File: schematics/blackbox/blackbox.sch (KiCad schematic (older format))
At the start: 37 parts

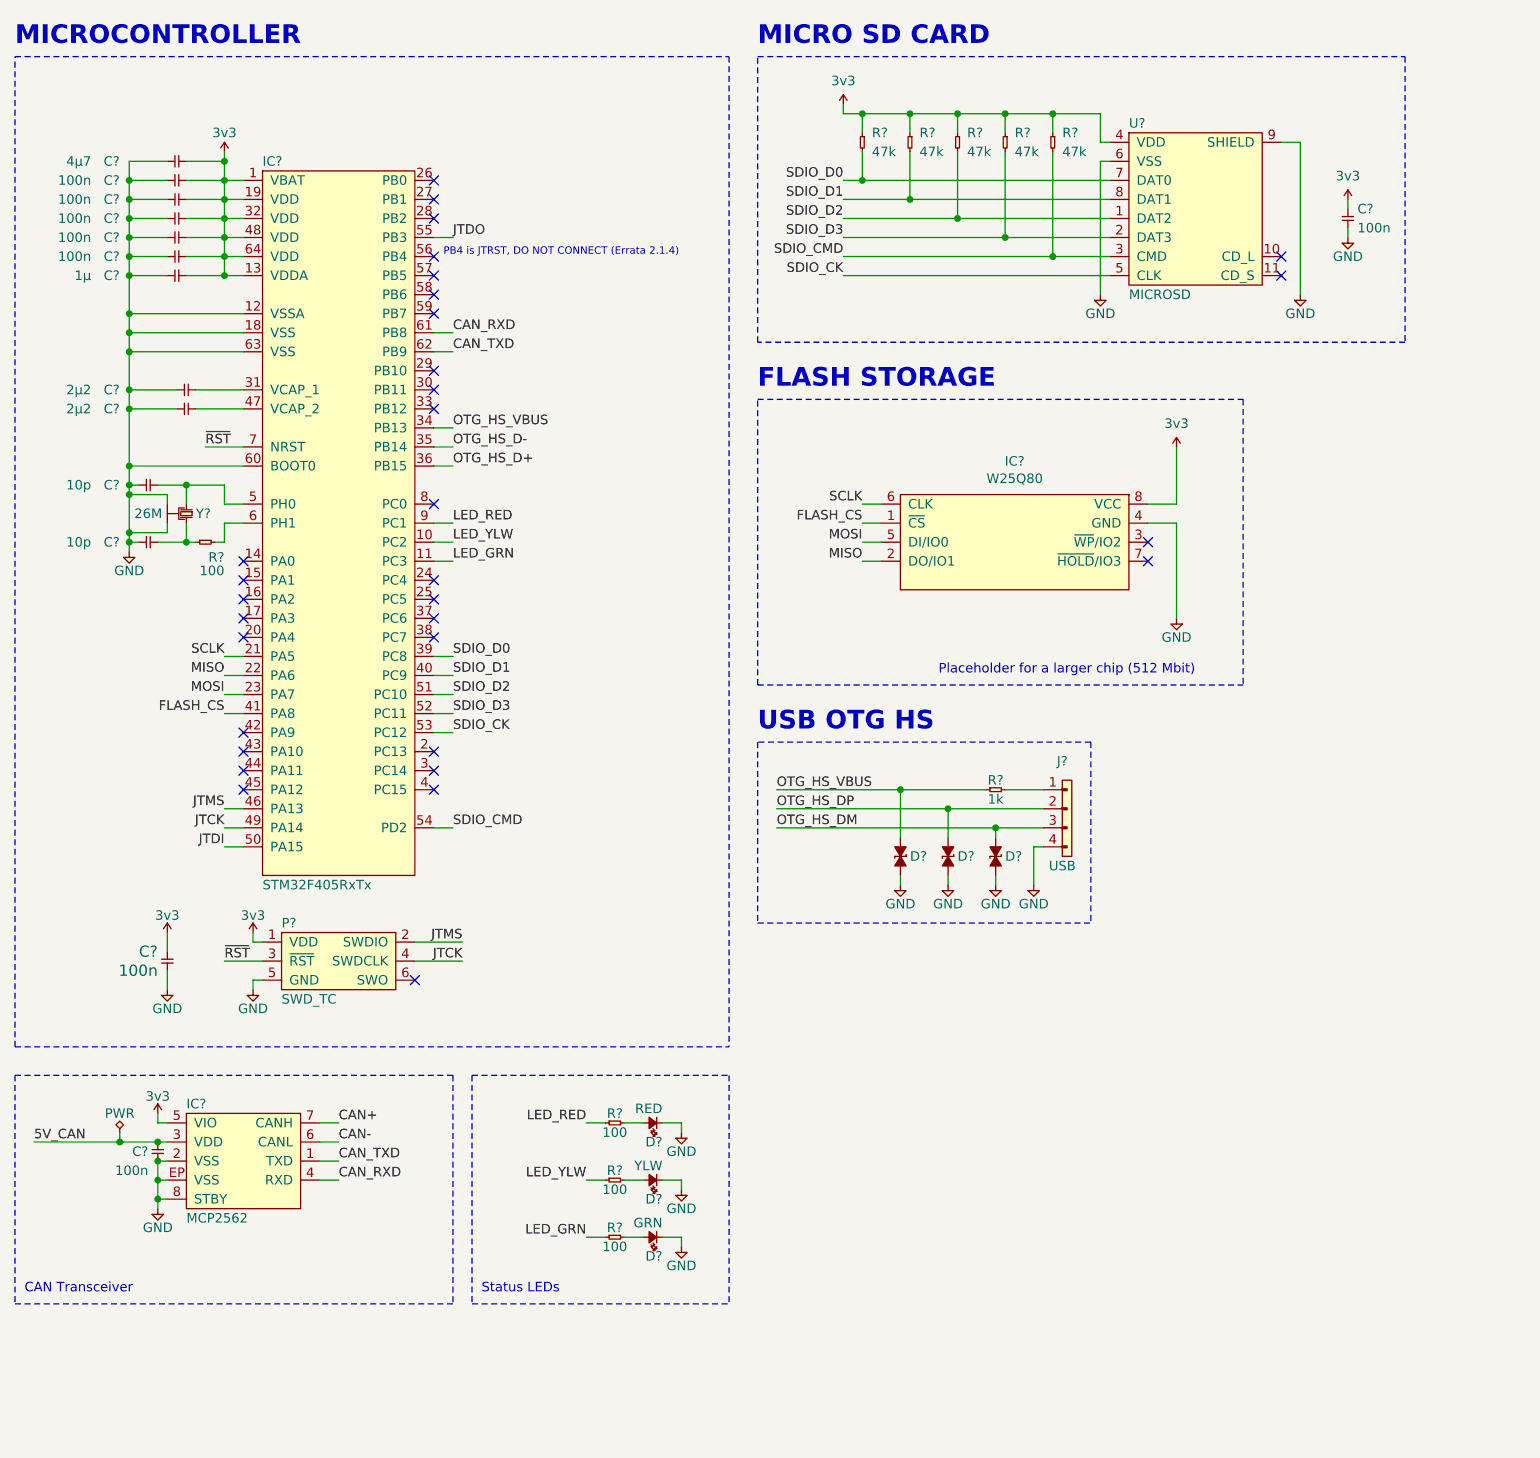
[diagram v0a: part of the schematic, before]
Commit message: Move dl to blackbox; fix minor errors in fc
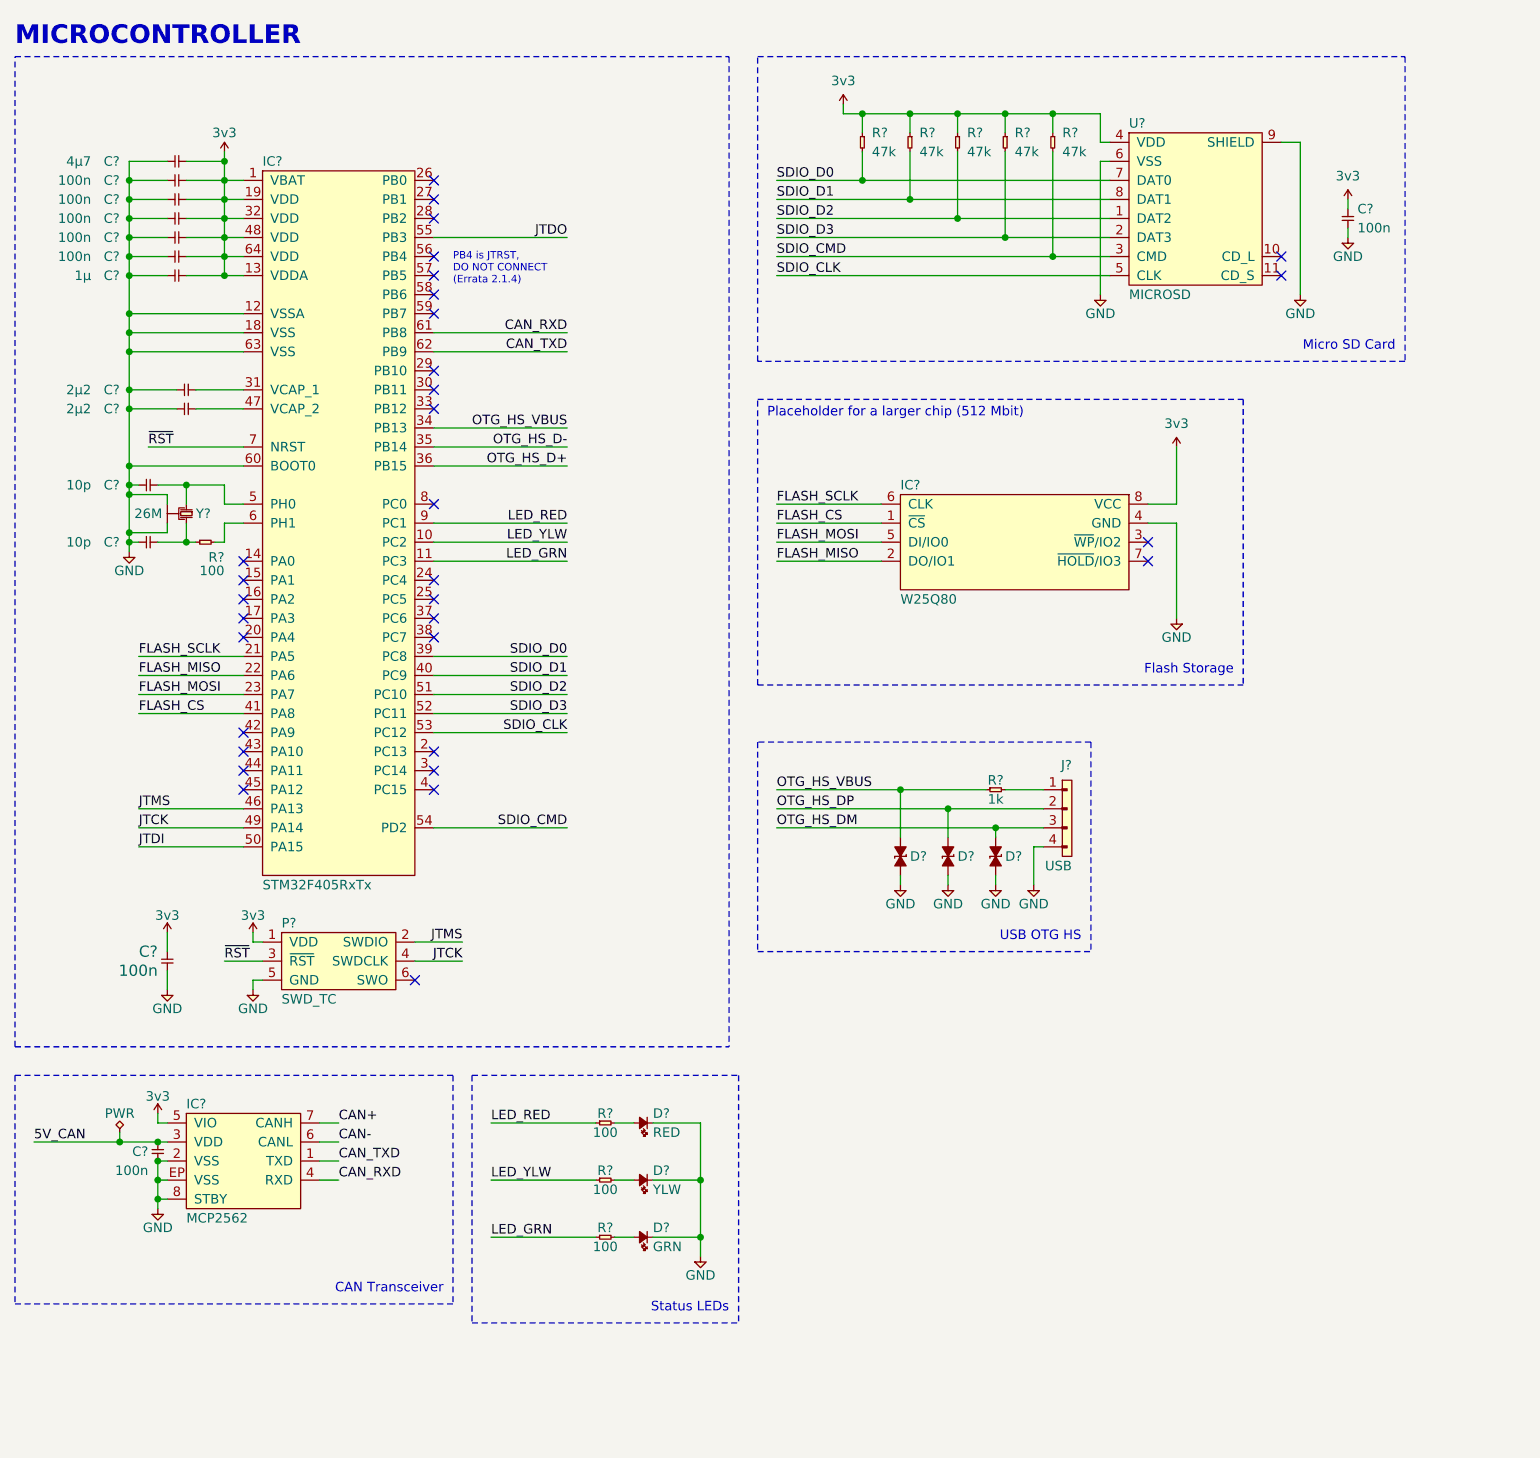
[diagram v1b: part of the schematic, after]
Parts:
- removed D?: YLW, agg:0603-LED, symbol cusf-kicad:LED
- removed D?: GRN, agg:0603-LED, symbol cusf-kicad:LED
- added D?: YLW, agg:0603-LED, symbol cusf-kicad:LED
- added D?: GRN, agg:0603-LED, symbol cusf-kicad:LED
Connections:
- net GND: now also D?.1, D?.1
- net at R?.2: now also D?.2 (x2)
- net MISO renamed FLASH_MISO
- net MOSI renamed FLASH_MOSI
- net SCLK renamed FLASH_SCLK
- net SDIO_CK renamed SDIO_CLK
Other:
- note added: "Flash Storage"
- note added: "Micro SD Card"
- note added: "PB4 is JTRST,\nDO NOT CONNECT\n(Errata 2.1.4)"
- note removed: "FLASH STORAGE"
- note removed: "MICRO SD CARD"
- note removed: "PB4 is JTRST, DO NOT CONNECT (Errata 2.1.4)"
- moved on the sheet: D?, R?

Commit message: Complete redesign
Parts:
- removed C? (x7): 100n, agg:0402, symbol cusf-kicad:C
- removed C? (x2): 2µ2, agg:0402, symbol cusf-kicad:C
- removed C?: 1µ, agg:0402, symbol cusf-kicad:C
- removed C?: 4µ7, agg:0402, symbol cusf-kicad:C
- removed C? (x2): 10p, agg:0402, symbol cusf-kicad:C
- removed D? (x3): ESD_DIODE, cusf:0402, symbol cusf-kicad:ESD_DIODE
- removed D?: RED, agg:0603-LED, symbol cusf-kicad:LED
- removed D?: YLW, agg:0603-LED, symbol cusf-kicad:LED
- removed D?: GRN, agg:0603-LED, symbol cusf-kicad:LED
- removed IC?: STM32F405RxTx, agg:LQFP-64, symbol cusf-kicad:STM32F405RxTx
- removed IC?: MCP2562, agg:DFN-8-EP-MICROCHIP, symbol cusf-kicad:MCP2562
- removed J?: USB, symbol cusf-kicad:CONN_01x04
- removed P?: SWD_TC, agg:TC2030-NL, symbol cusf-kicad:SWD_TC
- removed R? (x4): 100, agg:0402, symbol cusf-kicad:R
- removed R?: 1k, symbol cusf-kicad:R
- removed Y?: 26M, agg:XTAL-20x16, symbol cusf-kicad:SMD_XTAL
- added C1: 100n, cusf:0402, symbol cusf-kicad:C
- added H1, H2, H3, H4: MountingHole_Pad, cusf:M3_MOUNT, symbol cusf-kicad:MountingHole_Pad
- added IC1: SN65LVDT14, cusf:TSSOP-20, symbol cusf-kicad:SN65LVDT14
- added J1: PWR, cusf:MOLEX-KK-254P-03, symbol cusf-kicad:CONN_01x03
- added J2: RJHSE-538x, cusf:RJHSE-538X, symbol cusf-kicad:RJHSE-538x
- C2: renamed from C?; footprint (none) -> cusf:0402
- R1, R2, R3, R4, R5: renamed from R?; footprint (none) -> cusf:0402
- U1: renamed from U?; footprint agg:MICROSD_MOLEX_503398-1892 -> cusf:MICROSD_MOLEX_503398-1892
- gave numbers to parts that had none: 1
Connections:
- net SDIO_CLK is gone; now on net SCLK: U1.5 (CLK)
- net SDIO_CMD is gone; now on net MOSI: R5.2, U1.3 (CMD)
- net SDIO_D0 is gone; now on net MISO: R1.2, U1.7 (DAT0)
- net 3v3: now also C1.1, IC1.13 (VCC), IC1.17 (VCC), J1.3
- net GND: now also C1.2, H1.1, H2.1, H3.1, H4.1, IC1.11 (GND), IC1.15 (GND), IC1.19 (GND), J1.1, J1.2, J2.10 (LED1_A), J2.11 (LED2_C), J2.12 (LED2_A), J2.9 (LED1_C), J2.S1 (SHIELD), J2.S2 (SHIELD)
- net FLASH_CS renamed ~CS2
- net ~CS2: now also J2.4
- net FLASH_MISO renamed MISO
- net MISO: now also IC1.12 (D5)
- net FLASH_MOSI renamed MOSI
- net MOSI: now also IC1.18 (R2)
- net FLASH_SCLK renamed SCLK
- net SCLK: now also IC1.20 (R1)
- net SDIO_D1: no longer names the net of R2.2, U1.8 (DAT1)
- net SDIO_D2: no longer names the net of R3.2, U1.1 (DAT2)
- net SDIO_D3 renamed ~CS1
- net ~CS1: now also J2.5
- new net MISO+: IC1.9 (Y5), J2.3 (RX+)
- new net MISO-: IC1.10 (Z5), J2.6 (RX-)
- new net MOSI+: IC1.3 (A2), J2.1 (TX+)
- new net MOSI-: IC1.4 (B2), J2.2 (TX-)
- new net SCLK+: IC1.1 (A1), J2.8
- new net SCLK-: IC1.2 (B1), J2.7
- no-connect marks 32 -> 10
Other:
- note added: "Data In (RJ45)"
- note added: "LVDS Transceiver"
- note added: "Mounting Holes"
- note added: "Power In (Molex)"
- note added: "RJ45 Connector"
- note added: "SPI Flash Storage"
- note added: "Storage Peripherals"
- note removed: "CAN Transceiver"
- note removed: "Flash Storage"
- note removed: "MICROCONTROLLER"
- note removed: "PB4 is JTRST,\nDO NOT CONNECT\n(Errata 2.1.4)"
- note removed: "Status LEDs"
- note removed: "USB OTG HS"
- moved on the sheet: C2, IC2, R1, R2, R3, R4, R5, U1
